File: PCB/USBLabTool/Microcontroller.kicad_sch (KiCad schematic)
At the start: 4 parts, among them U13 STM32H562RGTx

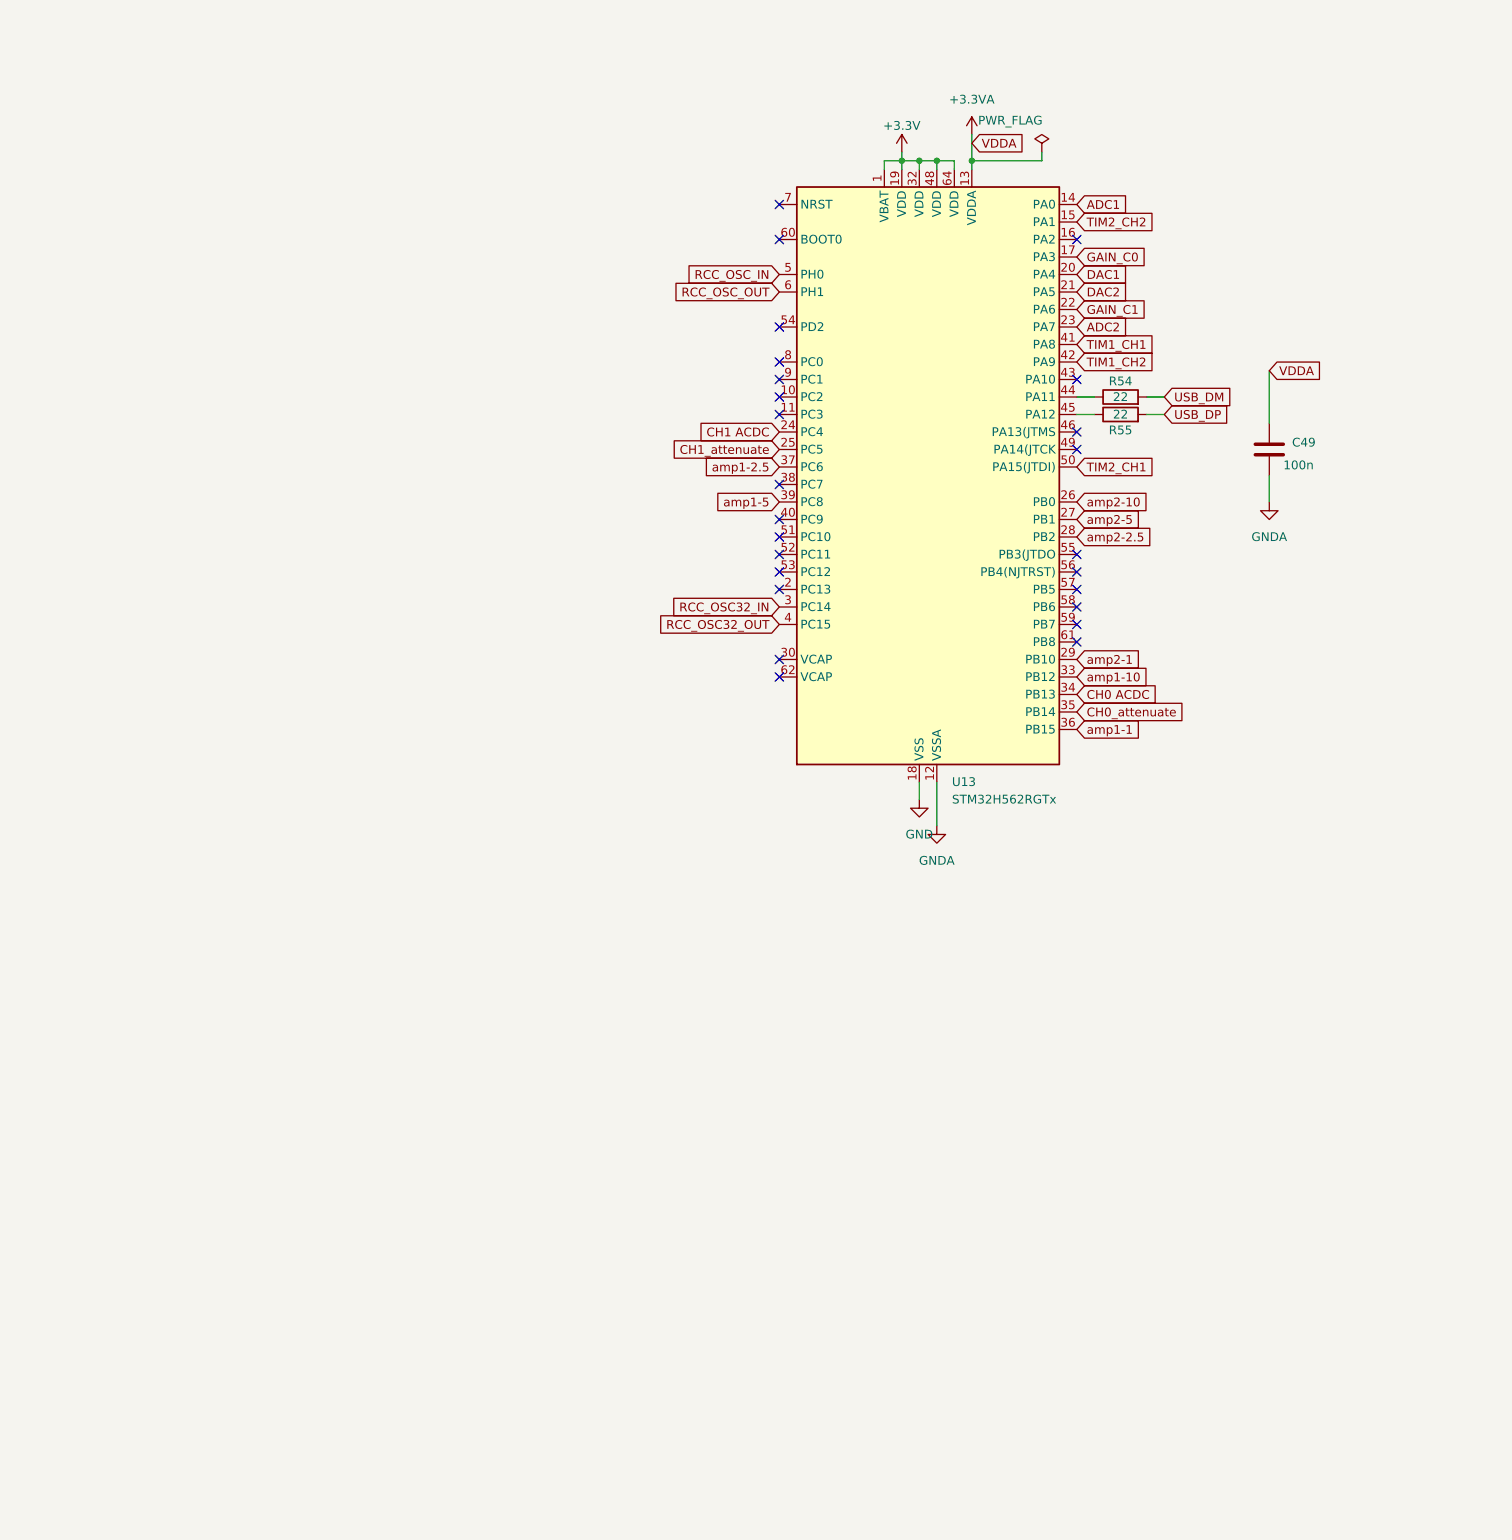
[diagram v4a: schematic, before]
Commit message: change USB design and MCU
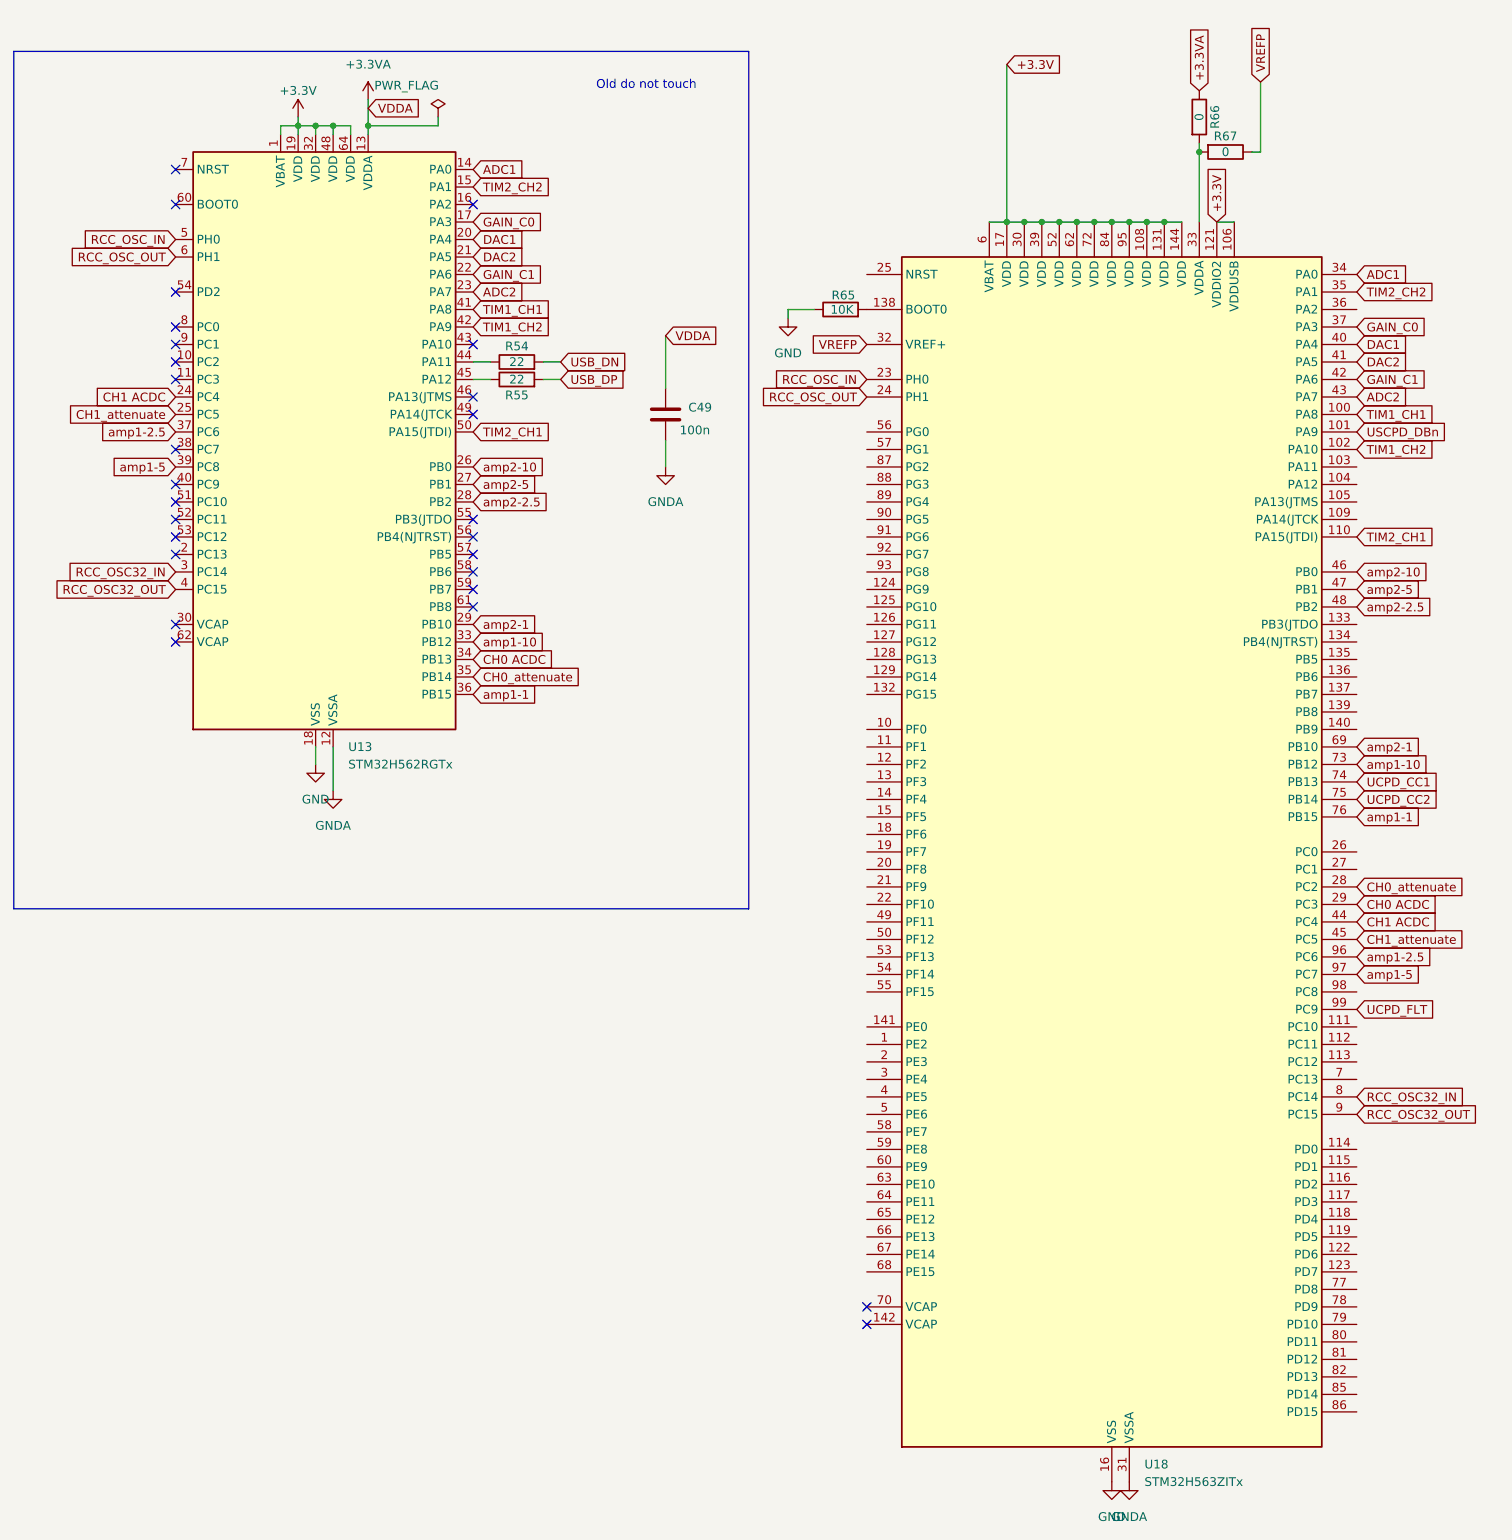
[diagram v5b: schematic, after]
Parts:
- added R65: 10K, Resistor_SMD:R_0603_1608Metric_Pad0.98x0.95mm_HandSolder, symbol Device:R
- added R66, R67: 0, Resistor_SMD:R_0603_1608Metric_Pad0.98x0.95mm_HandSolder, symbol Device:R
- added U18: STM32H563ZITx, Package_QFP:LQFP-144_20x20mm_P0.5mm, symbol MCU_ST_STM32H5:STM32H563ZITx
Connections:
- net +3.3V: now also U18.106 (VDDUSB), U18.108 (VDD), U18.121 (VDDIO2), U18.131 (VDD), U18.144 (VDD), U18.17 (VDD), U18.30 (VDD), U18.39 (VDD), U18.52 (VDD), U18.6 (VBAT), U18.62 (VDD), U18.72 (VDD), U18.84 (VDD), U18.95 (VDD)
- net +3.3VA: now also R66.1
- net ADC1: now also U18.34 (PA0)
- net ADC2: now also U18.43 (PA7)
- net CH0 ACDC: now also U18.29 (PC3)
- net CH0_attenuate: now also U18.28 (PC2)
- net CH1 ACDC: now also U18.44 (PC4)
- net CH1_attenuate: now also U18.45 (PC5)
- net DAC1: now also U18.40 (PA4)
- net DAC2: now also U18.41 (PA5)
- net GAIN_C0: now also U18.37 (PA3)
- net GAIN_C1: now also U18.42 (PA6)
- net GND: now also R65.1, U18.107 (VSS), U18.120 (VSS), U18.130 (VSS), U18.143 (VSS), U18.16 (VSS), U18.38 (VSS), U18.51 (VSS), U18.61 (VSS), U18.71 (VSS), U18.83 (VSS), U18.94 (VSS)
- net GNDA: now also U18.31 (VSSA)
- net RCC_OSC32_IN: now also U18.8 (PC14)
- net RCC_OSC32_OUT: now also U18.9 (PC15)
- net RCC_OSC_IN: now also U18.23 (PH0)
- net RCC_OSC_OUT: now also U18.24 (PH1)
- net TIM1_CH1: now also U18.100 (PA8)
- net TIM1_CH2: now also U18.102 (PA10)
- net TIM2_CH1: now also U18.110 (PA15(JTDI))
- net TIM2_CH2: now also U18.35 (PA1)
- net amp1-1: now also U18.76 (PB15)
- net amp1-10: now also U18.73 (PB12)
- net amp1-2.5: now also U18.96 (PC6)
- net amp1-5: now also U18.97 (PC7)
- net amp2-1: now also U18.69 (PB10)
- net amp2-10: now also U18.46 (PB0)
- net amp2-2.5: now also U18.48 (PB2)
- net amp2-5: now also U18.47 (PB1)
- net USB_DM renamed USB_DN
- new net: R65.2, U18.138 (BOOT0)
- new net: R66.2, R67.2, U18.33 (VDDA)
- new net UCPD_CC1: U18.74 (PB13)
- new net UCPD_CC2: U18.75 (PB14)
- new net UCPD_FLT: U18.99 (PC9)
- new net USCPD_DBn: U18.101 (PA9)
- new net VREFP: R67.1, U18.32 (VREF+)
- no-connect marks 25 -> 27
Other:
- note added: "Old do not touch"
- moved on the sheet: C49, R54, R55, U13
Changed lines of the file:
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@@
 	(generator "eeschema")
 	(generator_version "8.0")
-	(paper "A4")
+	(paper "A3")

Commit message: update MCU and USB, fix some footprints
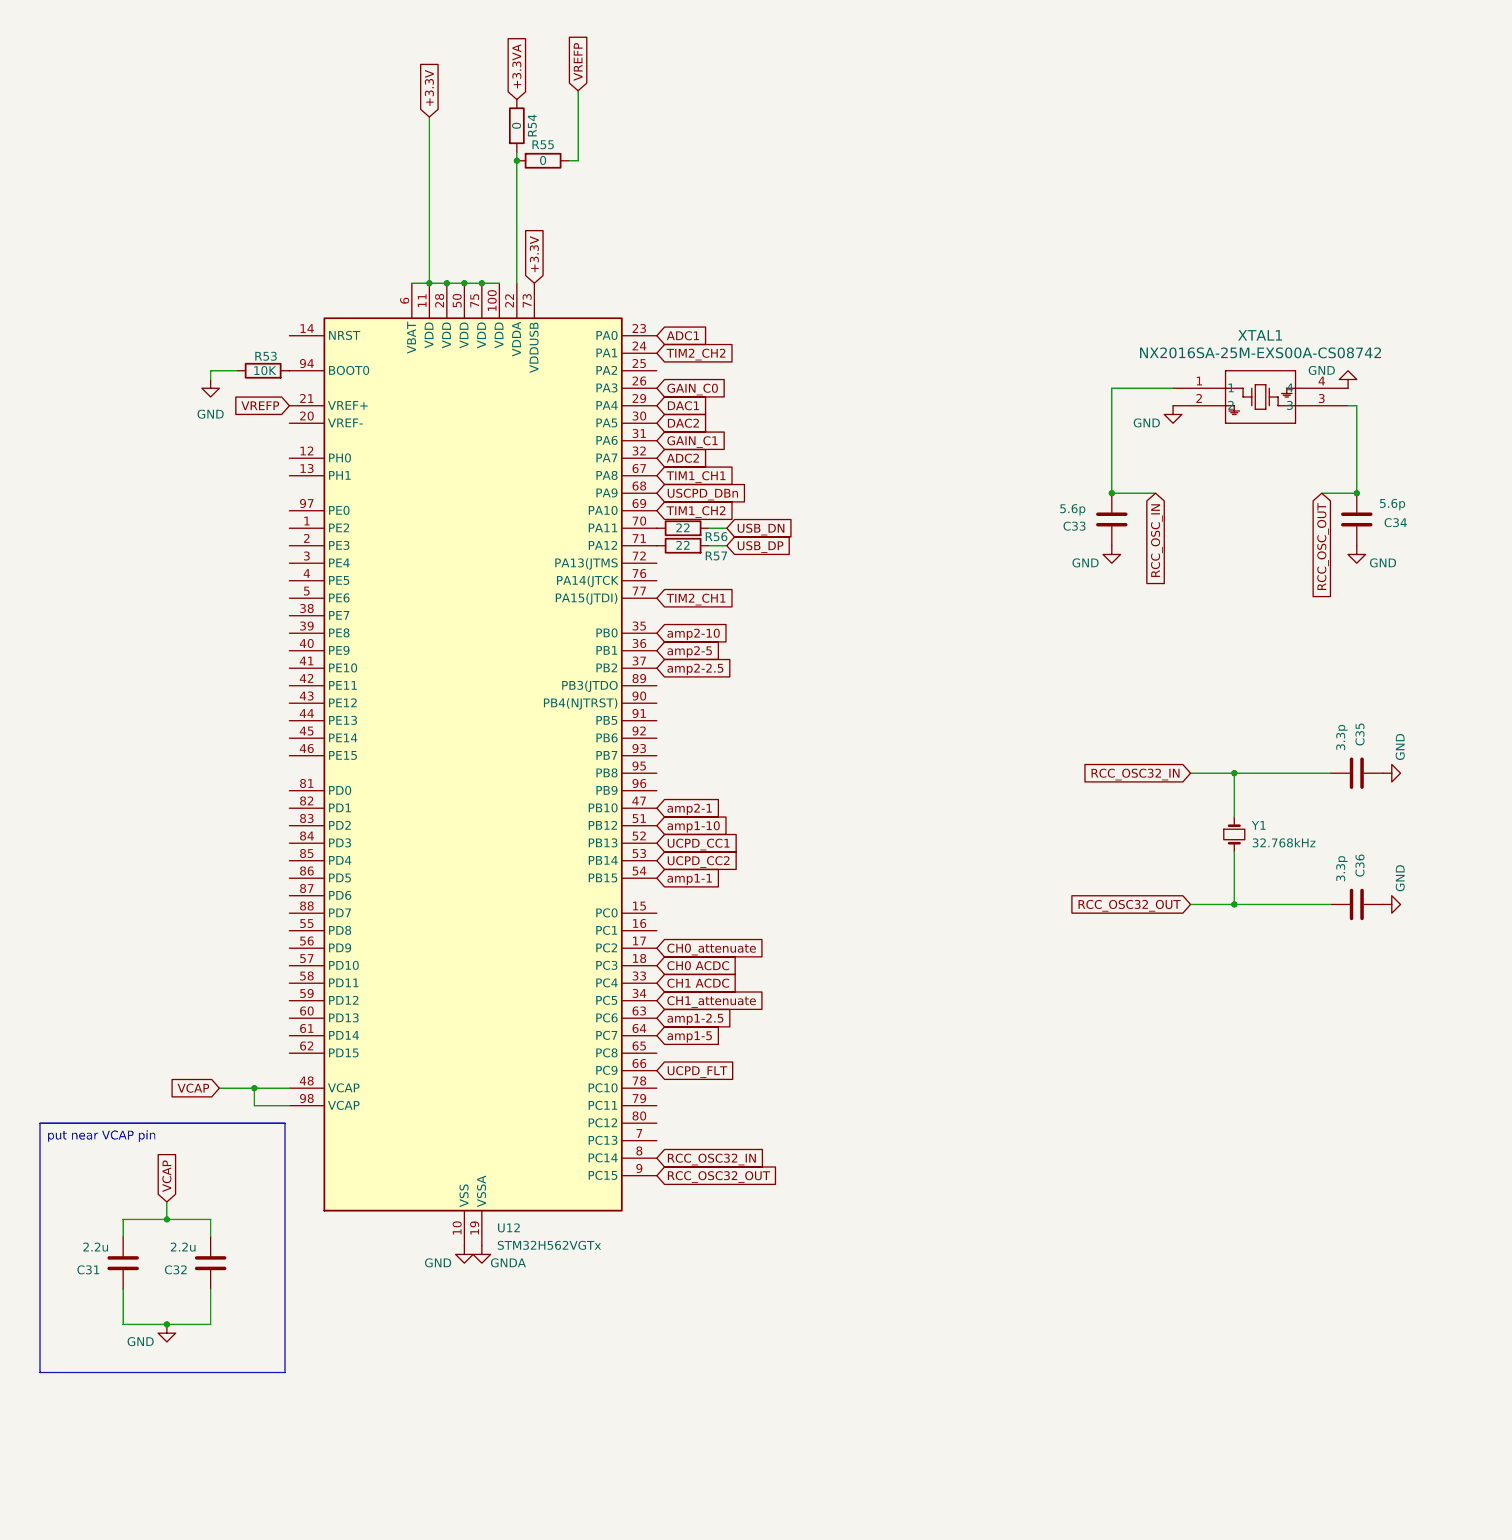
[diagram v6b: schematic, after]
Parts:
- removed C49: 100n, Capacitor_SMD:C_0603_1608Metric_Pad1.08x0.95mm_HandSolder, symbol Device:C
- removed R65: 10K, Resistor_SMD:R_0603_1608Metric_Pad0.98x0.95mm_HandSolder, symbol Device:R
- removed R66, R67: 0, Resistor_SMD:R_0603_1608Metric_Pad0.98x0.95mm_HandSolder, symbol Device:R
- removed U13: STM32H562RGTx, Package_QFP:LQFP-64_10x10mm_P0.5mm, symbol MCU_ST_STM32H5:STM32H562RGTx
- removed U18: STM32H563ZITx, Package_QFP:LQFP-144_20x20mm_P0.5mm, symbol MCU_ST_STM32H5:STM32H563ZITx
- added C31, C32: 2.2u, Diode_SMD:D_0805_2012Metric_Pad1.15x1.40mm_HandSolder, symbol Device:C
- added C33, C34: 5.6p, Capacitor_SMD:C_0201_0603Metric_Pad0.64x0.40mm_HandSolder, symbol Device:C
- added C35, C36: 3.3p, Capacitor_SMD:C_0201_0603Metric_Pad0.64x0.40mm_HandSolder, symbol Device:C
- added R53: 10K, Resistor_SMD:R_0603_1608Metric, symbol Device:R
- added R56, R57: 22, Resistor_SMD:R_0603_1608Metric_Pad0.98x0.95mm_HandSolder, symbol Device:R
- added U12: STM32H562VGTx, Package_QFP:LQFP-100_14x14mm_P0.5mm, symbol MCU_ST_STM32H5:STM32H562VGTx
- added XTAL1: NX2016SA-25M-EXS00A-CS08742, footprintsgit:NX2016SA_NDK, symbol NX2016SA-25MHz-20pF:NX2016SA-25M-EXS00A-CS08742
- added Y1: 32.768kHz, SparkFun-Clock:Crystal_SMD_3.2x1.5mm, symbol SparkFun-Clock:Crystal_32.768kHz_3.2x1.5mm
- R54, R55: value 22 -> 0
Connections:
- net +3.3V: now also U12.100 (VDD), U12.11 (VDD), U12.28 (VDD), U12.50 (VDD), U12.6 (VBAT), U12.73 (VDDUSB), U12.75 (VDD)
- net +3.3VA: now also R54.1
- net ADC1: now also U12.23 (PA0)
- net ADC2: now also U12.32 (PA7)
- net CH0 ACDC: now also U12.18 (PC3)
- net CH0_attenuate: now also U12.17 (PC2)
- net CH1 ACDC: now also U12.33 (PC4)
- net CH1_attenuate: now also U12.34 (PC5)
- net DAC1: now also U12.29 (PA4)
- net DAC2: now also U12.30 (PA5)
- net GAIN_C0: now also U12.26 (PA3)
- net GAIN_C1: now also U12.31 (PA6)
- net GND: now also C31.1, C32.1, C33.2, C34.1, C35.1, C36.1, R53.1, U12.10 (VSS), U12.27 (VSS), U12.49 (VSS), U12.74 (VSS), U12.99 (VSS), XTAL1.2, XTAL1.4
- net GNDA: now also U12.19 (VSSA)
- net RCC_OSC32_IN: now also C35.2, U12.8 (PC14), Y1.1
- net RCC_OSC32_OUT: now also C36.2, U12.9 (PC15), Y1.2
- net RCC_OSC_IN: now also C33.1, XTAL1.1
- net RCC_OSC_OUT: now also C34.2, XTAL1.3
- net TIM1_CH1: now also U12.67 (PA8)
- net TIM1_CH2: now also U12.69 (PA10)
- net TIM2_CH1: now also U12.77 (PA15(JTDI))
- net TIM2_CH2: now also U12.24 (PA1)
- net UCPD_CC1: now also U12.52 (PB13)
- net UCPD_CC2: now also U12.53 (PB14)
- net UCPD_FLT: now also U12.66 (PC9)
- net USB_DN: now also R56.2; no longer R54.2
- net USB_DP: now also R57.2; no longer R55.2
- net USCPD_DBn: now also U12.68 (PA9)
- net VREFP: now also R55.1, U12.21 (VREF+)
- net amp1-1: now also U12.54 (PB15)
- net amp1-10: now also U12.51 (PB12)
- net amp1-2.5: now also U12.63 (PC6)
- net amp1-5: now also U12.64 (PC7)
- net amp2-1: now also U12.47 (PB10)
- net amp2-10: now also U12.35 (PB0)
- net amp2-2.5: now also U12.37 (PB2)
- net amp2-5: now also U12.36 (PB1)
- new net: R54.2, R55.2, U12.22 (VDDA)
- new net: R56.1, U12.70 (PA11)
- new net: R57.1, U12.71 (PA12)
- new net: R53.2, U12.94 (BOOT0)
- new net VCAP: C31.2, C32.2, U12.48 (VCAP), U12.98 (VCAP)
- no-connect marks 27 -> 0
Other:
- note removed: "Old do not touch"
